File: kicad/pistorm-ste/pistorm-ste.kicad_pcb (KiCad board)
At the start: 4 copper layers, 105.5 x 44.2 mm, 33 parts, among them J1 Raspberry_Pi_2_3, J2 Conn_01x02_Male, U1 SN54CBTD3384, U2 SN74LVC16373, U3 SN74LVC16373, U4 EPM240T100, U5 SN74LVC16373, U6 SN74LVC16373, U7 SN54CBTD3384, U8 LM1117-3.3

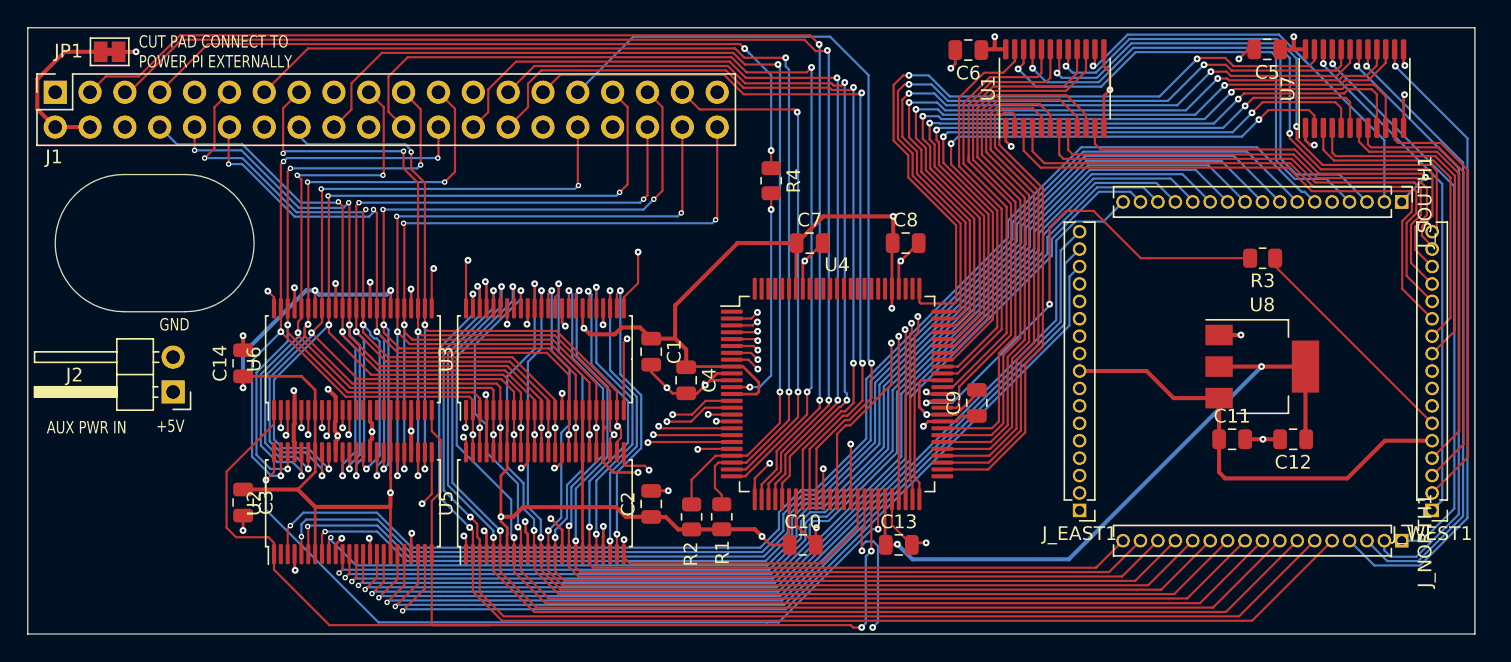
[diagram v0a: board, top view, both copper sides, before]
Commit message: Changing separate pin headers for PLCC plug footprint. DRC not passing yet
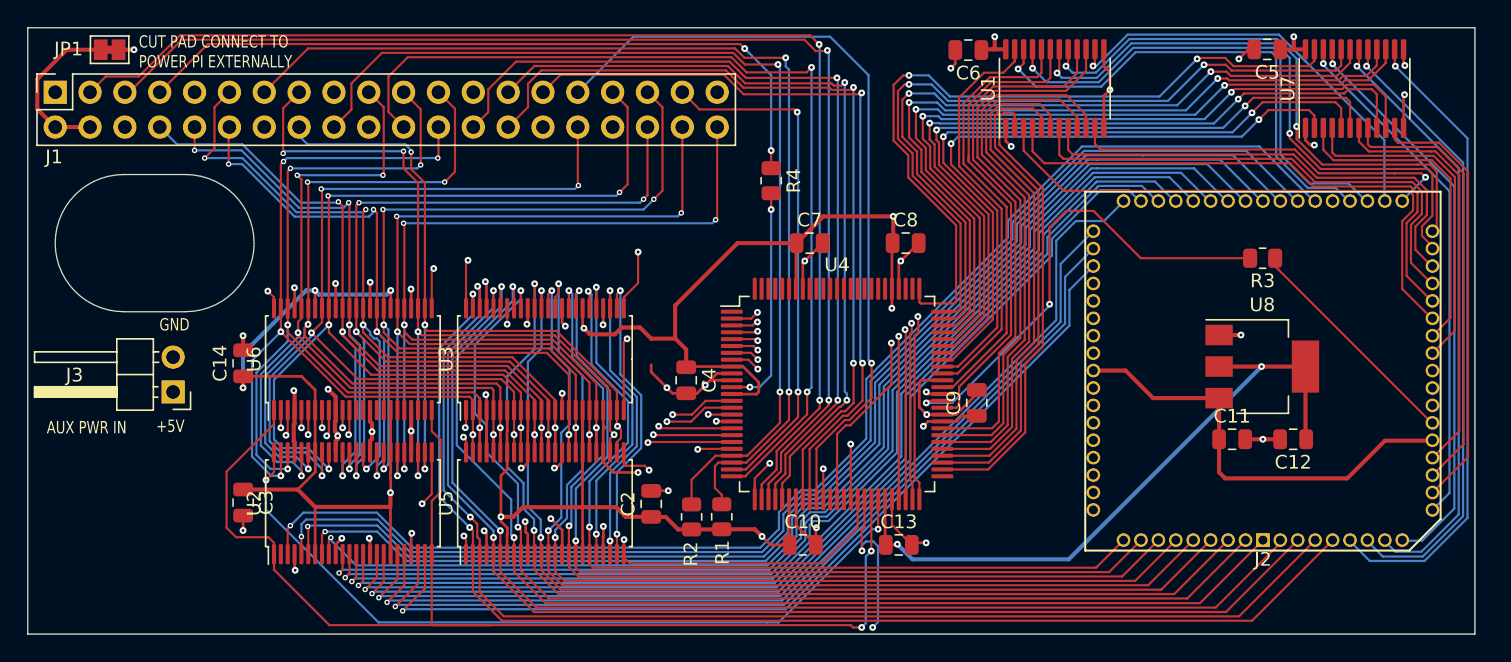
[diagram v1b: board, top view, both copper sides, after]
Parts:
- removed C1: 100n, Capacitor_SMD:C_0805_2012Metric
- removed J_EAST1, J_NORTH1, J_SOUTH1, J_WEST1: Conn_01x17_Male, Connector_PinHeader_1.27mm:PinHeader_1x17_P1.27mm_Vertical
- added J2: PLCC68_plug, PLCC_plugs:PLCC68_male_pins, F.Cu at (149.2, 152.1)
- moved JP1 0.15 mm to (65.1, 116.3)
- renumbered J2 to J3
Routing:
- net +5V: track 201.3 -> 199.5 mm
- net /A16: track 81.1 -> 82.1 mm
- net /A17: track 80.7 -> 81.7 mm
- net /D13: track 63.5 -> 64.5 mm
- net /A18: track 77.6 -> 78.6 mm
- net /LDS: track 44.6 -> 43.9 mm

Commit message: Passing DRC. Fixed 3d model issue with the plug footprint.
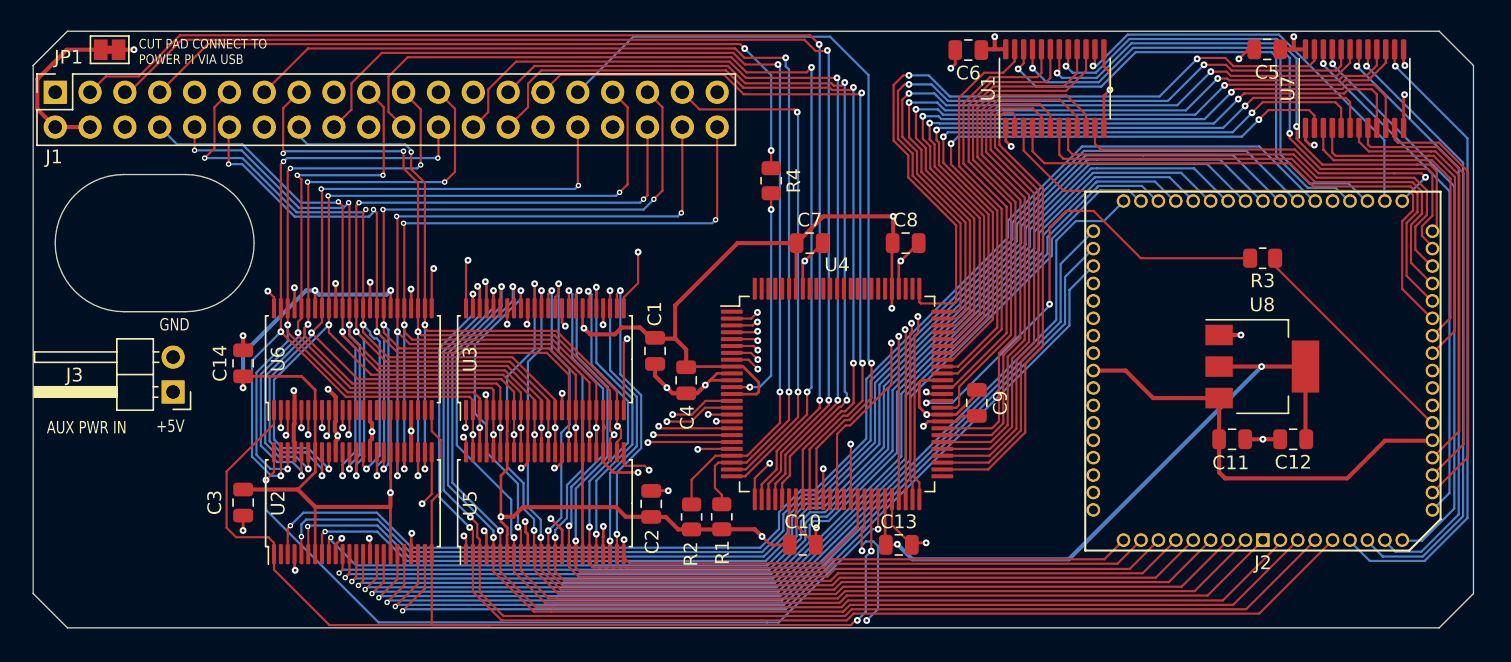
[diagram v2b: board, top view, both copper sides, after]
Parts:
- added C1: 100n, Capacitor_SMD:C_0805_2012Metric, F.Cu at (104.8, 138.3)
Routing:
- net /FC2: track 32.6 -> 31.1 mm
- net /SD6: track 80.7 -> 79.6 mm
- net /ADDR_LTCH_8: track 52.4 -> 51.4 mm
- net /ADDR_OE: track 90.5 -> 89.9 mm
- net /A19: track 77.4 -> 77.9 mm
- net /A20: track 74.5 -> 75.1 mm
- net /A21: track 72.9 -> 73.4 mm
- net /A22: track 69.7 -> 70.2 mm
- net /A23: track 68.1 -> 68.6 mm
- net /D15: track 62.8 -> 63.4 mm
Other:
- board size 105.5 x 44.2 mm -> 105 x 43.5 mm
- board text added: "CUT PAD CONNECT TO POWER PI VIA USB"
- board text removed: "CUT PAD CONNECT TO POWER PI EXTERNALLY"

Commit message: Adding a support post hole.
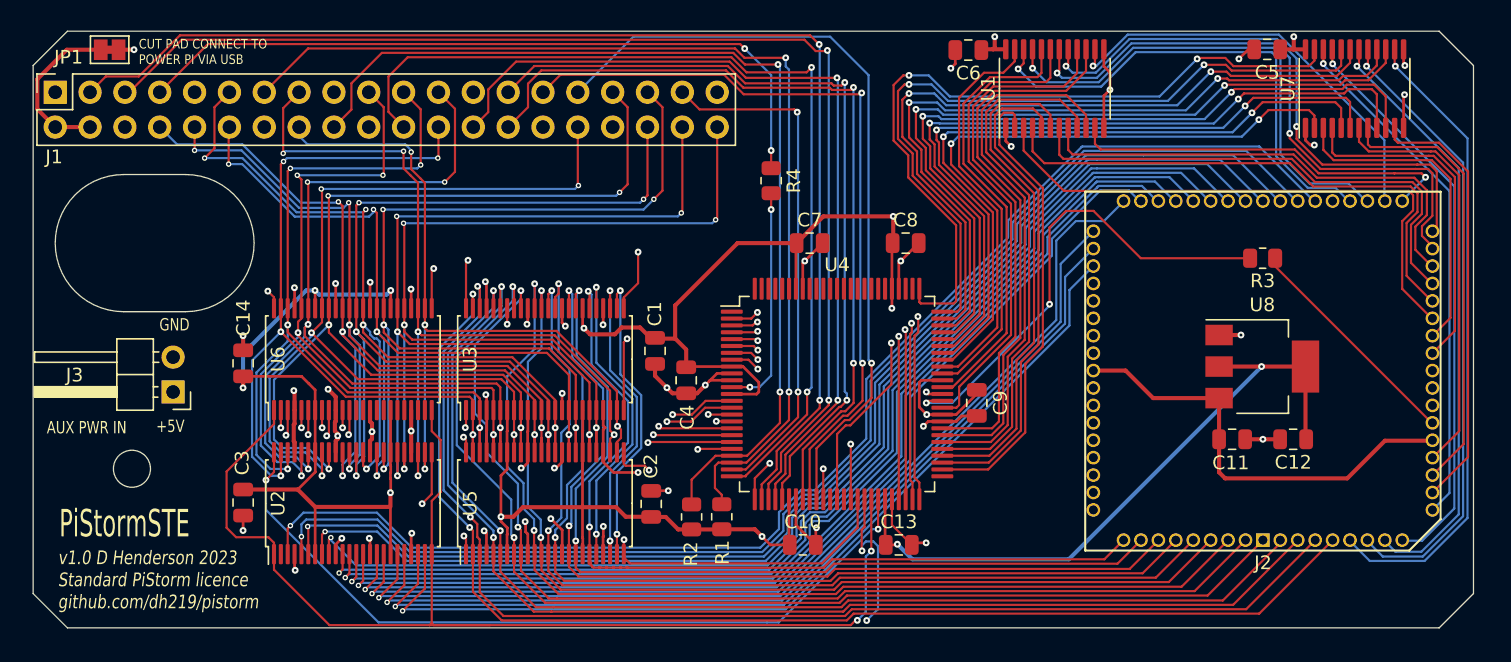
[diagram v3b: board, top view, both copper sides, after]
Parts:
- added REF**: MountingHole_2.7mm, MountingHole:MountingHole_2.7mm, F.Cu at (66.7, 146.9)
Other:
- board text added: "PiStormSTE"
- board text added: "v1.0 D Henderson 2023 Standard PiStorm licence github.com/dh219/pistorm"
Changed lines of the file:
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@@
   )
   (paper "A4")
+  (title_block
+    (title "PiStorm STE")
+    (date "2023-09-06")
+    (rev "1.0")
+    (company "D Henderson")
+    (comment 1 "Standard PiStorm Licence")
+  )
   (layers
     (0 "F.Cu" signal)
@@
       (outputformat 1)
       (mirror false)
-      (drillshape 1)
+      (drillshape 0)
       (scaleselection 1)
-      (outputdirectory "")
+      (outputdirectory "v1.0")
     )
   )
@@
     (property "Sheetname" "")
     (attr smd)
-    (fp_text reference "C2" (at -2.75 0.07 90) (layer "F.SilkS")
+    (fp_text reference "C2" (at 2.75 -0.03 90) (layer "F.SilkS")
       (effects (font (size 1 1) (thickness 0.15)))
     )
@@
     (property "Sheetname" "")
     (attr smd)
-    (fp_text reference "C3" (at 0 2.07 -270) (layer "F.SilkS")
+    (fp_text reference "C3" (at -2.9 0.07 -270) (layer "F.SilkS")
       (effects (font (size 1 1) (thickness 0.15)))
     )
@@
     (property "Sheetname" "")
     (attr smd)
-    (fp_text reference "C14" (at 0 -1.68 90) (layer "F.SilkS")
+    (fp_text reference "C14" (at 3.3 0.02 90) (layer "F.SilkS")
       (effects (font (size 1 1) (thickness 0.15)))
     )
@@
       (net 55 "/D5") (pinfunction "Pin_68") (pintype "passive"))
   )
+  (footprint "MountingHole:MountingHole_2.7mm" (layer "F.Cu")
+    (at 66.7 146.9)
+    (descr "Mounting Hole 2.7mm, no annular")
+    (tags "mounting hole 2.7mm no annular")
+    (attr exclude_from_pos_files exclude_from_bom)
+    (fp_text reference "REF**" (at -5.2 0) (layer "F.Fab")
+      (effects (font (size 1 1) (thickness 0.15)))
+    )
+    (fp_text value "MountingHole_2.7mm" (at 0 3.7) (layer "F.Fab")
+      (effects (font (size 1 1) (thickness 0.15)))
+    )
+    (fp_text user "${REFERENCE}" (at 0 0) (layer "F.Fab")
+      (effects (font (size 1 1) (thickness 0.15)))
+    )
+    (fp_circle (center 0 0) (end 2.7 0) (layer "Cmts.User") (width 0.15) (fill none))
+    (fp_circle (center 0 0) (end 2.95 0) (layer "F.CrtYd") (width 0.05) (fill none))
+    (pad "" np_thru_hole circle (at 0 0) (size 2.7 2.7) (drill 2.7) (layers *.Cu *.Mask))
+  )
   (footprint "Resistor_SMD:R_0805_2012Metric" (layer "F.Cu")
     (at 149.13 131.55 180)
@@
     (fp_line (start -1 -0.625) (end 1 -0.625) (layer "F.Fab") (width 0.1))
     (fp_line (start 1 0.625) (end -1 0.625) (layer "F.Fab") (width 0.1))
-    (pad "1" smd roundrect (at -0.9125 0 180) (size 1.025 1.4) (layers "F.Cu" "F.Paste" "F.Mask") (roundrect_rratio 0.243902)
+    (pad "1" smd roundrect (at -0.9125 0 180) (size 1.025 1.4) (layers "F.Cu" "F.Paste" "F.Mask") (roundrect_rratio 0.243902439)
       (net 160 "/CLK_STE") (pintype "passive"))
-    (pad "2" smd roundrect (at 0.9125 0 180) (size 1.025 1.4) (layers "F.Cu" "F.Paste" "F.Mask") (roundrect_rratio 0.243902)
+    (pad "2" smd roundrect (at 0.9125 0 180) (size 1.025 1.4) (layers "F.Cu" "F.Paste" "F.Mask") (roundrect_rratio 0.243902439)
       (net 91 "/CLK") (pintype "passive"))
     (model "${KICAD6_3DMODEL_DIR}/Resistor_SMD.3dshapes/R_0805_2012Metric.wrl"
@@
     (fp_line (start -1 0.625) (end -1 -0.625) (layer "F.Fab") (width 0.1))
     (fp_line (start 1 -0.625) (end 1 0.625) (layer "F.Fab") (width 0.1))
-    (pad "1" smd roundrect (at -0.9125 0 90) (size 1.025 1.4) (layers "F.Cu" "F.Paste" "F.Mask") (roundrect_rratio 0.243902)
+    (pad "1" smd roundrect (at -0.9125 0 90) (size 1.025 1.4) (layers "F.Cu" "F.Paste" "F.Mask") (roundrect_rratio 0.243902439)
       (net 2 "+3V3") (pintype "passive"))
-    (pad "2" smd roundrect (at 0.9125 0 90) (size 1.025 1.4) (layers "F.Cu" "F.Paste" "F.Mask") (roundrect_rratio 0.243902)
+    (pad "2" smd roundrect (at 0.9125 0 90) (size 1.025 1.4) (layers "F.Cu" "F.Paste" "F.Mask") (roundrect_rratio 0.243902439)
       (net 21 "/TMS") (pintype "passive"))
     (model "${KICAD6_3DMODEL_DIR}/Resistor_SMD.3dshapes/R_0805_2012Metric.wrl"
@@
     (fp_line (start 1 -0.625) (end 1 0.625) (layer "F.Fab") (width 0.1))
     (fp_line (start -1 -0.625) (end 1 -0.625) (layer "F.Fab") (width 0.1))
-    (pad "1" smd roundrect (at -0.9125 0 270) (size 1.025 1.4) (layers "F.Cu" "F.Paste" "F.Mask") (roundrect_rratio 0.243902)
+    (pad "1" smd roundrect (at -0.9125 0 270) (size 1.025 1.4) (layers "F.Cu" "F.Paste" "F.Mask") (roundrect_rratio 0.243902439)
       (net 162 "/PICLK_OUT") (pintype "passive"))
-    (pad "2" smd roundrect (at 0.9125 0 270) (size 1.025 1.4) (layers "F.Cu" "F.Paste" "F.Mask") (roundrect_rratio 0.243902)
+    (pad "2" smd roundrect (at 0.9125 0 270) (size 1.025 1.4) (layers "F.Cu" "F.Paste" "F.Mask") (roundrect_rratio 0.243902439)
       (net 30 "/PICLK") (pintype "passive"))
     (model "${KICAD6_3DMODEL_DIR}/Resistor_SMD.3dshapes/R_0805_2012Metric.wrl"
@@
     (fp_line (start 1 -0.625) (end 1 0.625) (layer "F.Fab") (width 0.1))
     (fp_line (start 1 0.625) (end -1 0.625) (layer "F.Fab") (width 0.1))
-    (pad "1" smd roundrect (at -0.9125 0 90) (size 1.025 1.4) (layers "F.Cu" "F.Paste" "F.Mask") (roundrect_rratio 0.243902)
+    (pad "1" smd roundrect (at -0.9125 0 90) (size 1.025 1.4) (layers "F.Cu" "F.Paste" "F.Mask") (roundrect_rratio 0.243902439)
       (net 2 "+3V3") (pintype "passive"))
-    (pad "2" smd roundrect (at 0.9125 0 90) (size 1.025 1.4) (layers "F.Cu" "F.Paste" "F.Mask") (roundrect_rratio 0.243902)
+    (pad "2" smd roundrect (at 0.9125 0 90) (size 1.025 1.4) (layers "F.Cu" "F.Paste" "F.Mask") (roundrect_rratio 0.243902439)
       (net 25 "/TDI") (pintype "passive"))
     (model "${KICAD6_3DMODEL_DIR}/Resistor_SMD.3dshapes/R_0805_2012Metric.wrl"
@@
   (gr_arc (start 70.60538 125.44868) (mid 75.60538 130.44868) (end 70.60538 135.44868) (layer "Edge.Cuts") (width 0.05))
   (gr_line (start 162 158.5) (end 164.5 156) (layer "Edge.Cuts") (width 0.05))
+  (gr_text "v1.0 D Henderson 2023\nStandard PiStorm licence\ngithub.com/dh219/pistorm" (at 61.3 155) (layer "F.SilkS")
+    (effects (font (size 1 0.8) (thickness 0.2) italic) (justify left))
+  )
   (gr_text "+5V" (at 69.5 143.8) (layer "F.SilkS")
     (effects (font (size 0.9 0.7) (thickness 0.175)))
   )
+  (gr_text "PiStormSTE" (at 61.4 150.9) (layer "F.SilkS")
+    (effects (font (size 2 1.2) (thickness 0.3)) (justify left))
+  )
   (gr_text "GND" (at 69.8 136.4) (layer "F.SilkS")
     (effects (font (size 0.9 0.7) (thickness 0.175)))
@@
   (segment (start 120.75 152.2) (end 120.205096 152.2) (width 0.16) (layer "B.Cu") (net 107))
   (segment (start 119.924119 152.480977) (end 119.924119 152.883622) (width 0.16) (layer "B.Cu") (net 107))
-  (segment (start 88.55541 158.25541) (end 88.6 158.3) (width 0.16) (layer "F.Cu") (net 108))
   (segment (start 89.2 144.8) (end 88.55541 144.15541) (width 0.16) (layer "F.Cu") (net 108))
+  (segment (start 88.41082 158.3) (end 88.55541 158.15541) (width 0.16) (layer "F.Cu") (net 108))
+  (segment (start 88.55541 158.15541) (end 88.7 158.3) (width 0.16) (layer "F.Cu") (net 108))
   (segment (start 74.29 151.89) (end 73.6 151.2) (width 0.16) (layer "F.Cu") (net 108))
+  (segment (start 81.1 158.3) (end 88.4 158.3) (width 0.16) (layer "F.Cu") (net 108))
   (segment (start 77.05541 152.29541) (end 76.65 151.89) (width 0.16) (layer "F.Cu") (net 108))
   (segment (start 76.65 151.89) (end 74.29 151.89) (width 0.16) (layer "F.Cu") (net 108))
   (segment (start 88.55541 149.24459) (end 89.2 148.6) (width 0.16) (layer "F.Cu") (net 108))
   (segment (start 89.2 148.6) (end 89.2 144.8) (width 0.16) (layer "F.Cu") (net 108))
-  (segment (start 88.55541 153.125062) (end 88.55541 158.25541) (width 0.16) (layer "F.Cu") (net 108))
   (segment (start 77.05541 153.125062) (end 77.05541 152.29541) (width 0.16) (layer "F.Cu") (net 108))
   (segment (start 77.05541 153.125062) (end 77.05541 154.25541) (width 0.16) (layer "F.Cu") (net 108))
-  (segment (start 88.6 158.3) (end 92.8 158.3) (width 0.16) (layer "F.Cu") (net 108))
+  (segment (start 88.4 158.3) (end 88.41082 158.3) (width 0.16) (layer "F.Cu") (net 108))
+  (segment (start 88.7 158.3) (end 92.8 158.3) (width 0.16) (layer "F.Cu") (net 108))
   (segment (start 73.6 151.2) (end 73.6 147.1) (width 0.16) (layer "F.Cu") (net 108))
   (segment (start 88.55541 153.125062) (end 88.55541 149.24459) (width 0.16) (layer "F.Cu") (net 108))
@@
   (segment (start 119.4505 157.9495) (end 119.1 158.3) (width 0.16) (layer "F.Cu") (net 108))
   (segment (start 119.1 158.3) (end 92.8 158.3) (width 0.16) (layer "F.Cu") (net 108))
+  (segment (start 88.4 158.3) (end 92.8 158.3) (width 0.16) (layer "F.Cu") (net 108))
+  (segment (start 88.55541 153.125062) (end 88.55541 158.15541) (width 0.16) (layer "F.Cu") (net 108))
   (segment (start 77.05541 143.64459) (end 77.05541 142.625062) (width 0.16) (layer "F.Cu") (net 108))
-  (segment (start 81.1 158.3) (end 92.8 158.3) (width 0.16) (layer "F.Cu") (net 108))
   (segment (start 120.6 149.12906) (end 120.60538 149.12368) (width 0.16) (layer "F.Cu") (net 108))
   (via (at 119.582595 157.9495) (size 0.5) (drill 0.2) (layers "F.Cu" "B.Cu") (net 108))

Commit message: Squeezed down to 100mm width to fit in the PCBWay cheaper bracket
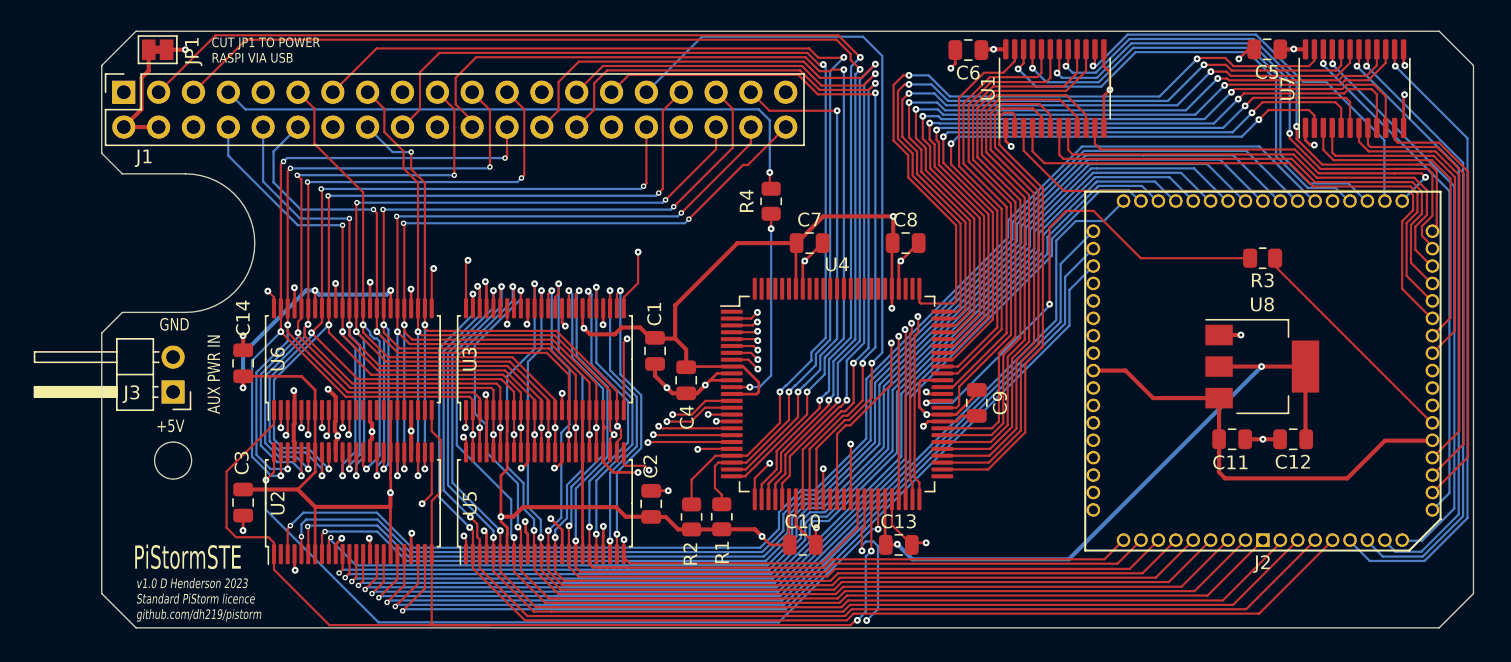
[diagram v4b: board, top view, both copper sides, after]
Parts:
- moved J1 5.00 mm to (66.1, 119.4)
- moved JP1 3.50 mm to (68.6, 116.3)
- moved REF** 3.06 mm to (69.7, 146.3)
- moved R4 1.50 mm to (113.3, 127.4)
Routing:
- net /SD9: track 76.5 -> 67.9 mm, vias 6 -> 4
- net /PICLK_OUT: track 53.8 -> 45.2 mm, vias 2 -> 1
- net /SD14: track 68.8 -> 60.4 mm, vias 6 -> 4
- net +5V: track 199.5 -> 193.9 mm
- net /SD15: track 63.3 -> 57.9 mm
- net /SD2: track 85.5 -> 90.7 mm
- net /SD3: track 88.9 -> 94.1 mm
- net /SD1: track 88.2 -> 93.3 mm
- net /SD0: track 87.8 -> 92.7 mm
- net /SD4: track 94.6 -> 99.4 mm
- net /SD6: track 79.6 -> 75.0 mm
- net /SD7: track 72.4 -> 67.8 mm, vias 6 -> 5
- net /SA0: track 55.9 -> 52.2 mm
- net /SD11: track 88.7 -> 92.1 mm
- net /+5V_PI: track 12.1 -> 8.93 mm
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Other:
- board size 105 x 43.5 mm -> 100 x 43.5 mm
- board text added: "CUT JP1 TO POWER RASPI VIA USB"
- board text removed: "CUT PAD CONNECT TO POWER PI VIA USB"
